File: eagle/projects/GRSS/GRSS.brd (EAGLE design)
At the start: 85 x 47 mm, 33 parts, among them J1 MOL-SL-2-RA, J10 MOL-SL-2-RA, J11 M02PTH, J2 MOL-SL-2-RA, J3 MOL-SL-2-RA, J4 MOL-SL-2-RA, J5 MOL-SL-2-RA, J6 MOL-SL-2-RA, J7 MOL-SL-2-RA, J8 MOL-SL-2-RA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

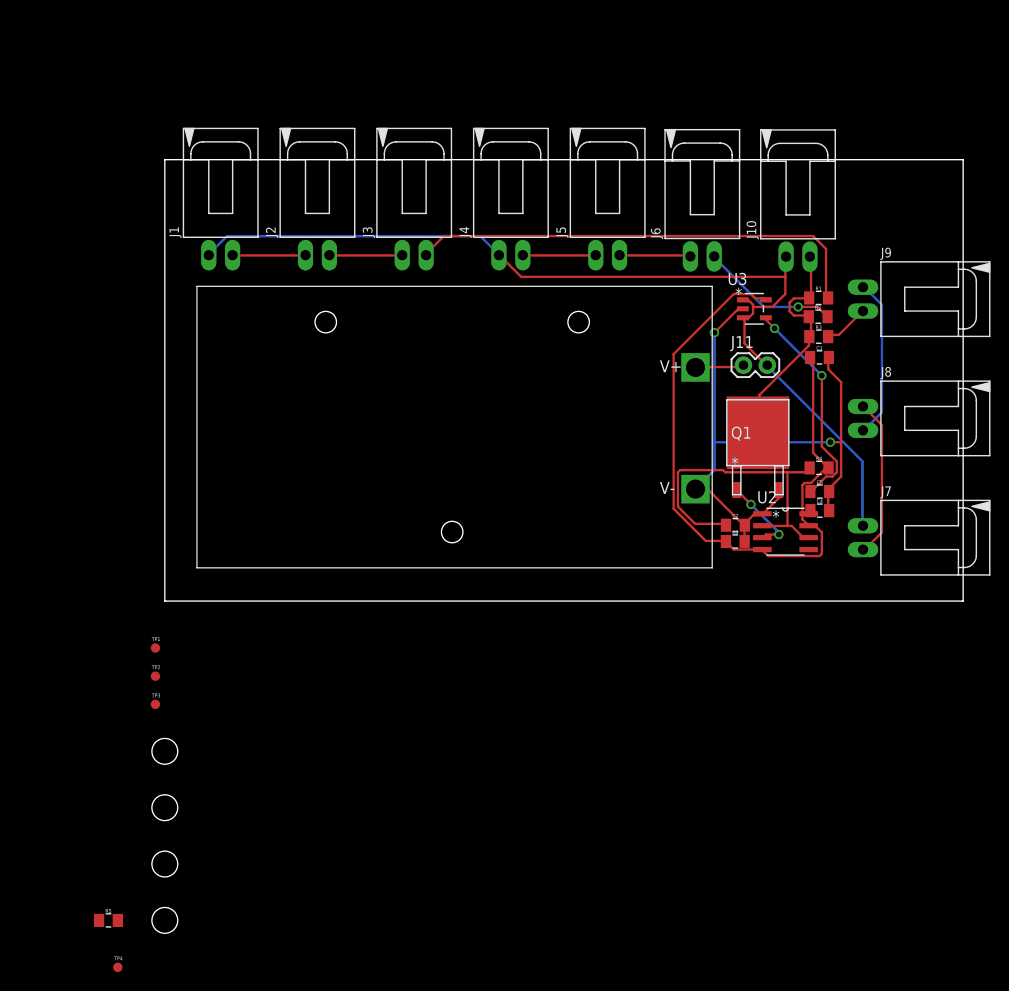
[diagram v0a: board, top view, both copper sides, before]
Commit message: Added 3.3,4.7uF,1k to lib, Schematic now at RevB, Battery flipped to bottom of board
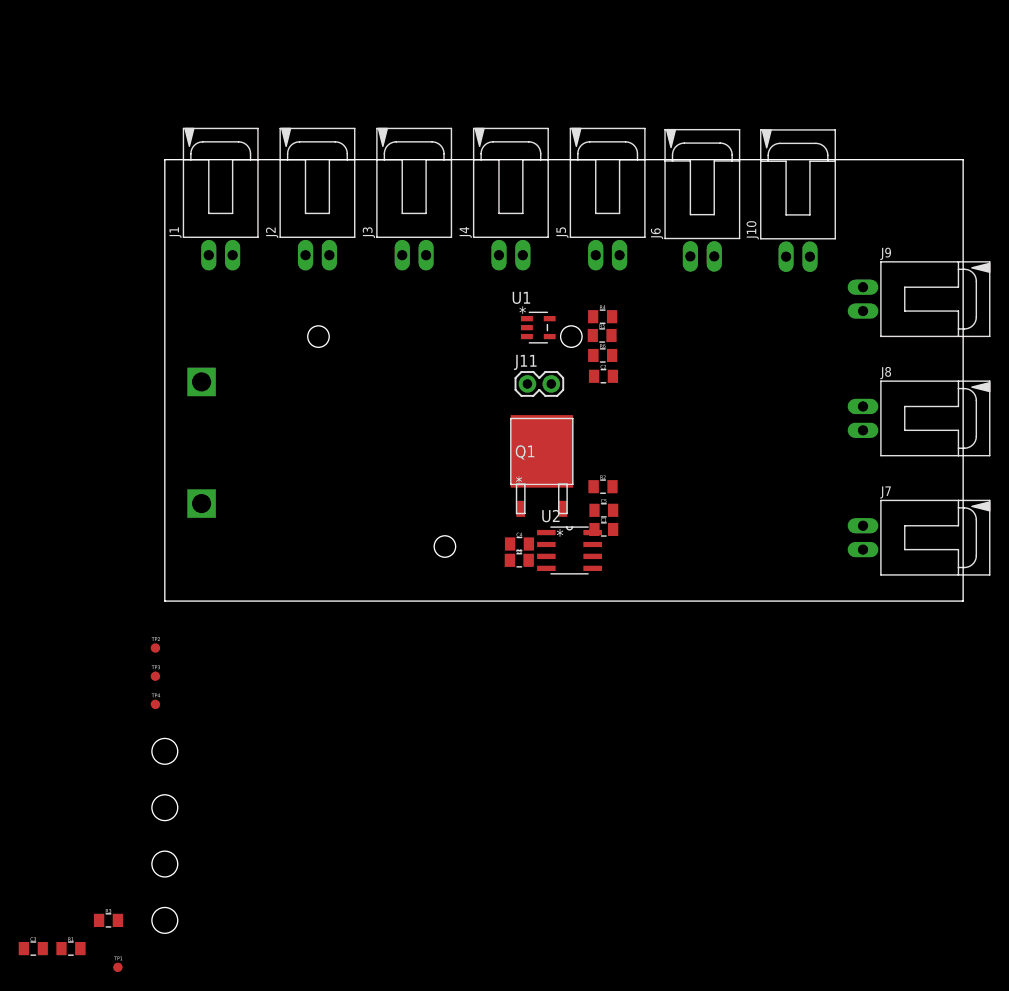
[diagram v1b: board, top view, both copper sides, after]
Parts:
- removed U3: LP2985AIM5-4.5/NOPB, grss:MF05A
- added C6: 3.3uF, grss:C0805
- added R6: 100, grss:R0805
- added U1: LP2985AIM5-4.5/NOPB, grss:MF05A
- C1: value 0.1uF -> 1uF
- C2: value 10uF -> 0.1uF
- C3: value 2.2uF -> 1uF
- C4: value 1uF -> 10uF
- R1: value 100 -> 1k
- R2: value 100 -> 470k
- R3: value 100 -> 4.7k
- R4: value 240k -> 100
- R5: value 4.7k -> 100
- TP1: value (none) -> GND
- TP2: value (none) -> 4V5
- TP3: value (none) -> 555OUT
- TP4: value (none) -> VD
- moved R1 105.5 mm to (-10.0, -37.0)
- moved R3 97.9 mm to (-6.00, -34.0)
- moved C3 86.4 mm to (-14.0, -37.0)
- moved R5 81.5 mm to (46.6, 28.3)
- moved BATT 53.6 mm to (57.0, 2.00), flipped to the bottom
- moved TP1 34.2 mm to (-5.00, -39.0)
- moved C4 32.2 mm to (37.8, 6.07)
- moved C1 29.4 mm to (46.7, 7.63)
- moved R2 29.2 mm to (46.7, 12.2)
- moved TP4 28.3 mm to (-1.00, -11.0)
- moved R4 28.1 mm to (46.6, 30.3)
- moved J11 23.1 mm to (38.6, 23.1)
- moved Q1 23.1 mm to (40.1, 15.9)
- moved U2 23.1 mm to (43.1, 5.39)
- moved C5 23.1 mm to (46.7, 9.66)
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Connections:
- new net DIS: R1.1, R2.2, U2.7
- net 4V5: now also C2.1, C6.1, R1.2, TP2.TP, U1.5; no longer C1.1, R4.2, TP1.TP, U2.7, U3.5
- net 555OUT: now also R3.2, TP3.TP; no longer R5.2, TP2.TP
- net 9V0: now also C1.1, U1.1, U1.3; no longer C4.1, U3.1, U3.3
- net BP: now also U1.4; no longer U3.4
- net GND: now also C6.2, R3.1, TP1.TP, U1.2; no longer R5.1, TP4.TP, U3.2
- net RES123: now also R4.2; no longer R1.2
- net RES456: now also R5.2; no longer R2.2
- net RES789: now also R6.2; no longer R3.2
- net THRTRIG: now also C4.1, R2.1; no longer C2.1, R4.1
- net VD: now also R4.1, R5.1, R6.1, TP4.TP; no longer R1.1, R2.1, R3.1, TP3.TP
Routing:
- net 9V0: track 103.0 -> 0.00 mm
- net 4V5: track 71.9 -> 0.00 mm
- net GND: track 67.0 -> 0.00 mm, vias 2 -> 0
- net RES123: track 49.4 -> 0.00 mm
- net THRTRIG: track 35.7 -> 0.00 mm
- net VD: track 25.0 -> 0.00 mm
- net BP: track 23.2 -> 0.00 mm, vias 2 -> 0
- net LED78: track 17.0 -> 0.00 mm
- net LED89: track 17.0 -> 0.00 mm
- net RES456: track 14.8 -> 0.00 mm, vias 1 -> 0
- net 555OUT: track 8.47 -> 0.00 mm, vias 2 -> 0
- net LED45: track 7.77 -> 0.00 mm
- net LED23: track 7.77 -> 0.00 mm
- net LED12: track 7.77 -> 0.00 mm
- net LED56: track 7.57 -> 0.00 mm
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
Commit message: rough initial placement... 66x50mm
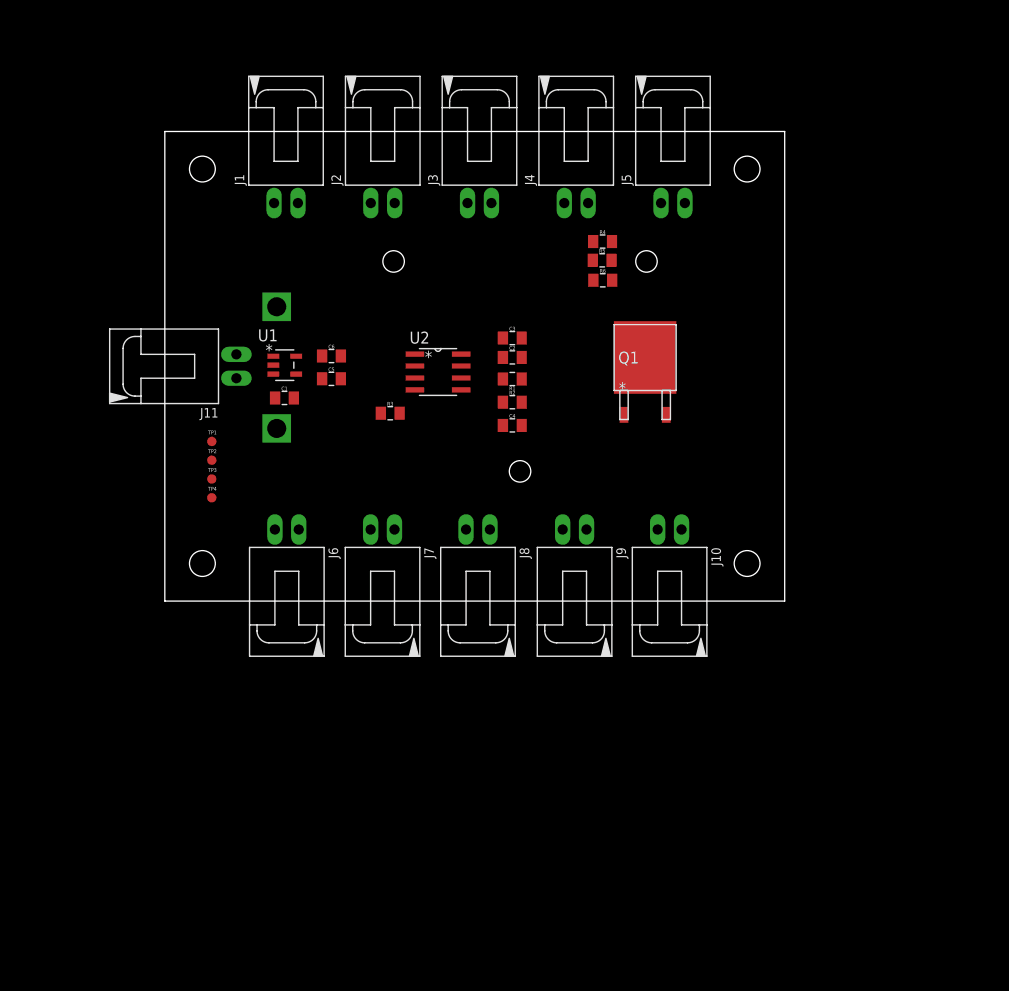
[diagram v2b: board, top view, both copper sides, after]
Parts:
- J11: value M02PTH -> MOL-SL-2-RA; device grss:1X02 -> grss:MOLSL-2-RA
- moved H4 101.2 mm to (62.0, 46.0)
- moved C3 82.6 mm to (37.0, 28.0)
- moved R1 76.7 mm to (37.0, 23.6), turned to 180 degrees
- moved H3 74.1 mm to (4.00, 46.0)
- moved H2 67.2 mm to (62.0, 4.00)
- moved J6 62.6 mm to (13.0, 0.00), turned to 180 degrees
- moved R3 61.8 mm to (24.0, 20.0)
- moved J7 59.2 mm to (23.2, 0.00), turned to 180 degrees
- moved TP1 56.9 mm to (5.00, 17.0)
- moved J8 52.4 mm to (33.3, 0.00), turned to 180 degrees
- moved J9 50.0 mm to (43.6, 0.00), turned to 180 degrees
- moved J10 46.4 mm to (53.7, 0.00), turned to 180 degrees
- moved J11 38.7 mm to (0.00, 25.0), turned to 90 degrees
- moved C1 36.8 mm to (12.7, 21.6)
- moved C5 32.2 mm to (17.7, 23.7)
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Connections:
- removed net 9V0SRC: BATT.V+, J11.1
- new net 9VSRC: BATT.V+, J11.2
- net 9V0: now also J11.1; no longer J11.2
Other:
- board size 85 x 47 mm -> 66 x 50 mm

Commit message: Updated LED series resistor to 200 ohms
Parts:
- R4, R5, R6: value 100 -> 200
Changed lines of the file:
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@@
 <attribute name="MANUFACTURER_PN" value="STD12NF06LT4" x="51.14" y="25.93" size="1.778" layer="27" display="off"/>
 </element>
-<element name="R4" library="grss" package="R0805" value="100" x="46.615" y="38.28">
+<element name="R4" library="grss" package="R0805" value="200" x="46.615" y="38.28">
 <attribute name="POWER" value="1/2W" x="46.615" y="38.28" size="1.778" layer="27" display="off"/>
-<attribute name="VENDOR_PN" value="P16057CT-ND" x="46.615" y="38.28" size="1.778" layer="27" display="off"/>
+<attribute name="VENDOR_PN" value="P16064CT-ND" x="46.615" y="38.28" size="1.778" layer="27" display="off"/>
 <attribute name="VENDOR" value="Digi-key" x="46.615" y="38.28" size="1.778" layer="27" display="off"/>
 <attribute name="MANUFACTURER" value="Panasonic" x="46.615" y="38.28" size="1.778" layer="27" display="off"/>
-<attribute name="MANUFACTURER_PN" value="ERJ-P06F1000V" x="46.615" y="38.28" size="1.778" layer="27" display="off"/>
+<attribute name="MANUFACTURER_PN" value="ERJ-P06F2000V" x="46.615" y="38.28" size="1.778" layer="27" display="off"/>
 <attribute name="TOLERANCE" value="1%" x="46.615" y="38.28" size="1.778" layer="27" display="off"/>
 </element>
-<element name="R5" library="grss" package="R0805" value="100" x="46.567" y="36.28">
+<element name="R5" library="grss" package="R0805" value="200" x="46.567" y="36.28">
 <attribute name="POWER" value="1/2W" x="46.567" y="36.28" size="1.778" layer="27" display="off"/>
-<attribute name="VENDOR_PN" value="P16057CT-ND" x="46.567" y="36.28" size="1.778" layer="27" display="off"/>
+<attribute name="VENDOR_PN" value="P16064CT-ND" x="46.567" y="36.28" size="1.778" layer="27" display="off"/>
 <attribute name="VENDOR" value="Digi-key" x="46.567" y="36.28" size="1.778" layer="27" display="off"/>
 <attribute name="MANUFACTURER" value="Panasonic" x="46.567" y="36.28" size="1.778" layer="27" display="off"/>
-<attribute name="MANUFACTURER_PN" value="ERJ-P06F1000V" x="46.567" y="36.28" size="1.778" layer="27" display="off"/>
+<attribute name="MANUFACTURER_PN" value="ERJ-P06F2000V" x="46.567" y="36.28" size="1.778" layer="27" display="off"/>
 <attribute name="TOLERANCE" value="1%" x="46.567" y="36.28" size="1.778" layer="27" display="off"/>
 </element>
-<element name="R6" library="grss" package="R0805" value="100" x="46.63" y="34.153">
+<element name="R6" library="grss" package="R0805" value="200" x="46.63" y="34.153">
 <attribute name="POWER" value="1/2W" x="46.63" y="34.153" size="1.778" layer="27" display="off"/>
-<attribute name="VENDOR_PN" value="P16057CT-ND" x="46.63" y="34.153" size="1.778" layer="27" display="off"/>
+<attribute name="VENDOR_PN" value="P16064CT-ND" x="46.63" y="34.153" size="1.778" layer="27" display="off"/>
 <attribute name="VENDOR" value="Digi-key" x="46.63" y="34.153" size="1.778" layer="27" display="off"/>
 <attribute name="MANUFACTURER" value="Panasonic" x="46.63" y="34.153" size="1.778" layer="27" display="off"/>
-<attribute name="MANUFACTURER_PN" value="ERJ-P06F1000V" x="46.63" y="34.153" size="1.778" layer="27" display="off"/>
+<attribute name="MANUFACTURER_PN" value="ERJ-P06F2000V" x="46.63" y="34.153" size="1.778" layer="27" display="off"/>
 <attribute name="TOLERANCE" value="1%" x="46.63" y="34.153" size="1.778" layer="27" display="off"/>
 </element>

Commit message: Added Zero ohm resistor on FET drain for sys current meas
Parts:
- added R7: 0.0, grss:R0805
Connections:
- new net ZEROOHM: Q1.2, R7.2
- net GND: now also R7.1; no longer Q1.2
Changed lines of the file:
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@@
 <attribute name="VENDOR" value="Digi-key" x="37" y="28" size="1.778" layer="27" display="off"/>
+</element>
+<element name="R7" library="grss" package="R0805" value="0.0" x="-8" y="-3">
+<attribute name="POWER" value="1/8W" x="-8" y="-3" size="1.778" layer="27" display="off"/>
+<attribute name="TOLERANCE" value="Jumper" x="-8" y="-3" size="1.778" layer="27" display="off"/>
+<attribute name="VENDOR" value="Digi-key" x="-8" y="-3" size="1.778" layer="27" display="off"/>
+<attribute name="MANUFACTURER" value="Panasonic" x="-8" y="-3" size="1.778" layer="27" display="off"/>
+<attribute name="MANUFACTURER_PN" value="ERJ-6GEY0R00V" x="-8" y="-3" size="1.778" layer="27" display="off"/>
+<attribute name="VENDOR_PN" value="P0.0ACT-ND" x="-8" y="-3" size="1.778" layer="27" display="off"/>
 </element>
 </elements>
@@
 <contactref element="C5" pad="2"/>
 <contactref element="C6" pad="2"/>
-<contactref element="Q1" pad="2"/>
 <contactref element="R3" pad="1"/>
 <contactref element="TP1" pad="TP"/>
@@
 <contactref element="C3" pad="2"/>
 <contactref element="C4" pad="2"/>
-<wire x1="11.5508" y1="25.12" x2="38" y2="25.944" width="0" layer="19" extent="1-1"/>
-<wire x1="18.74" y1="23.66" x2="38" y2="25.944" width="0" layer="19" extent="1-1"/>
+<contactref element="R7" pad="1"/>
+<wire x1="38" y1="25.944" x2="38" y2="28" width="0" layer="19" extent="1-1"/>
+<wire x1="38" y1="18.707" x2="38" y2="25.944" width="0" layer="19" extent="1-1"/>
+<wire x1="26.6262" y1="26.295" x2="38" y2="25.944" width="0" layer="19" extent="1-1"/>
+<wire x1="23" y1="20" x2="26.6262" y2="26.295" width="0" layer="19" extent="1-1"/>
+<wire x1="18.74" y1="23.66" x2="23" y2="20" width="0" layer="19" extent="1-1"/>
+<wire x1="18.745" y1="26.089" x2="18.74" y2="23.66" width="0" layer="19" extent="1-1"/>
 <wire x1="13.74" y1="21.628" x2="18.74" y2="23.66" width="0" layer="19" extent="1-1"/>
-<wire x1="53.39" y1="19.8213" x2="18.74" y2="23.66" width="0" layer="19" extent="1-1"/>
-<wire x1="26.6262" y1="26.295" x2="53.39" y2="19.8213" width="0" layer="19" extent="1-1"/>
-<wire x1="38" y1="18.707" x2="26.6262" y2="26.295" width="0" layer="19" extent="1-1"/>
-<wire x1="18.745" y1="26.089" x2="38" y2="18.707" width="0" layer="19" extent="1-1"/>
-<wire x1="11.914" y1="18.382" x2="38" y2="18.707" width="0" layer="19" extent="1-1"/>
-<wire x1="23" y1="20" x2="11.914" y2="18.382" width="0" layer="19" extent="1-1"/>
-<wire x1="5" y1="17" x2="23" y2="20" width="0" layer="19" extent="1-1"/>
-<wire x1="38" y1="28" x2="23" y2="20" width="0" layer="19" extent="1-1"/>
+<wire x1="11.914" y1="18.382" x2="13.74" y2="21.628" width="0" layer="19" extent="1-1"/>
+<wire x1="11.5508" y1="25.12" x2="13.74" y2="21.628" width="0" layer="19" extent="1-1"/>
+<wire x1="5" y1="17" x2="11.914" y2="18.382" width="0" layer="19" extent="1-1"/>
+<wire x1="-9" y1="-3" x2="5" y2="17" width="0" layer="19" extent="1-1"/>
 </signal>
 <signal name="THRTRIG">
@@
 <wire x1="11.914" y1="31.336" x2="7.62" y2="26.27" width="0" layer="19" extent="1-1"/>
 </signal>
+<signal name="ZEROOHM">
+<contactref element="R7" pad="2"/>
+<contactref element="Q1" pad="2"/>
+<wire x1="-7" y1="-3" x2="53.39" y2="19.8213" width="0" layer="19" extent="1-1"/>
+</signal>
 </signals>

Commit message: small placement change
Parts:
- moved R7 58.5 mm to (48.0, 14.0), turned to 90 degrees
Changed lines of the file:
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@@
 <attribute name="VENDOR" value="Digi-key" x="37" y="28" size="1.778" layer="27" display="off"/>
 </element>
-<element name="R7" library="grss" package="R0805" value="0.0" x="-8" y="-3">
-<attribute name="POWER" value="1/8W" x="-8" y="-3" size="1.778" layer="27" display="off"/>
-<attribute name="TOLERANCE" value="Jumper" x="-8" y="-3" size="1.778" layer="27" display="off"/>
-<attribute name="VENDOR" value="Digi-key" x="-8" y="-3" size="1.778" layer="27" display="off"/>
-<attribute name="MANUFACTURER" value="Panasonic" x="-8" y="-3" size="1.778" layer="27" display="off"/>
-<attribute name="MANUFACTURER_PN" value="ERJ-6GEY0R00V" x="-8" y="-3" size="1.778" layer="27" display="off"/>
-<attribute name="VENDOR_PN" value="P0.0ACT-ND" x="-8" y="-3" size="1.778" layer="27" display="off"/>
+<element name="R7" library="grss" package="R0805" value="0.0" x="48" y="14" rot="R90">
+<attribute name="POWER" value="1/8W" x="48" y="14" size="1.778" layer="27" rot="R90" display="off"/>
+<attribute name="TOLERANCE" value="Jumper" x="48" y="14" size="1.778" layer="27" rot="R90" display="off"/>
+<attribute name="VENDOR" value="Digi-key" x="48" y="14" size="1.778" layer="27" rot="R90" display="off"/>
+<attribute name="MANUFACTURER" value="Panasonic" x="48" y="14" size="1.778" layer="27" rot="R90" display="off"/>
+<attribute name="MANUFACTURER_PN" value="ERJ-6GEY0R00V" x="48" y="14" size="1.778" layer="27" rot="R90" display="off"/>
+<attribute name="VENDOR_PN" value="P0.0ACT-ND" x="48" y="14" size="1.778" layer="27" rot="R90" display="off"/>
 </element>
 </elements>
@@
 <wire x1="11.5508" y1="25.12" x2="13.74" y2="21.628" width="0" layer="19" extent="1-1"/>
 <wire x1="5" y1="17" x2="11.914" y2="18.382" width="0" layer="19" extent="1-1"/>
-<wire x1="-9" y1="-3" x2="5" y2="17" width="0" layer="19" extent="1-1"/>
+<wire x1="48" y1="13" x2="5" y2="17" width="0" layer="19" extent="1-1"/>
 </signal>
 <signal name="THRTRIG">
@@
 <contactref element="R7" pad="2"/>
 <contactref element="Q1" pad="2"/>
-<wire x1="-7" y1="-3" x2="53.39" y2="19.8213" width="0" layer="19" extent="1-1"/>
+<wire x1="48" y1="15" x2="53.39" y2="19.8213" width="0" layer="19" extent="1-1"/>
 </signal>
 </signals>

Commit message: Attempt at LDO / 555 Timer solo Layout
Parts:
- moved R3 10.8 mm to (28.0, 30.0), turned to 270 degrees
- moved C3 10.4 mm to (34.0, 38.0), turned to 180 degrees
- moved R2 9.65 mm to (43.8, 28.0), turned to 90 degrees
- moved C2 9.59 mm to (34.0, 35.1), turned to 180 degrees
- moved C4 8.68 mm to (41.7, 26.0), turned to 270 degrees
- moved R1 7.87 mm to (41.6, 30.0), turned to 90 degrees
- moved U2 7.07 mm to (34.1, 29.4)
- moved C5 6.36 mm to (24.0, 24.7), turned to 90 degrees
- moved U1 5.10 mm to (17.8, 26.1)
- moved C1 4.48 mm to (13.4, 26.1)
- moved C6 4.12 mm to (21.8, 26.7), turned to 270 degrees
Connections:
- net N$1 renamed NC
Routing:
- net 4V5: track 0.00 -> 24.2 mm, vias 0 -> 2
- net GND: track 0.00 -> 21.4 mm
- net THRTRIG: track 0.00 -> 13.5 mm
- net 9V0: track 0.00 -> 11.7 mm
- net LED45: track 0.00 -> 7.76 mm
- net LED23: track 0.00 -> 7.76 mm
- net LED12: track 0.00 -> 7.76 mm
- net DIS: track 0.00 -> 7.69 mm
- net BP: track 0.00 -> 5.70 mm
- net 555OUT: track 0.00 -> 3.73 mm

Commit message: LG Route Take 1
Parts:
- moved TP4 45.6 mm to (50.6, 11.7)
- moved TP2 26.0 mm to (28.3, 26.5)
- moved R5 24.8 mm to (41.1, 12.1), turned to 270 degrees
- moved TP3 24.7 mm to (29.4, 16.7)
- moved R6 22.2 mm to (44.1, 12.1), turned to 270 degrees
- moved R4 12.7 mm to (45.9, 25.6), turned to 90 degrees
- moved Q1 9.95 mm to (59.6, 20.7), turned to 270 degrees
- moved R2 6.73 mm to (45.9, 21.6)
- moved R3 6.65 mm to (29.4, 23.5)
- moved U2 6.62 mm to (35.4, 22.9)
- moved C2 6.61 mm to (35.4, 28.6)
- moved C3 6.55 mm to (35.4, 31.6)
- moved R1 6.52 mm to (42.9, 23.6)
- moved C4 6.51 mm to (42.9, 19.6)
- moved R7 4.72 mm to (49.6, 18.4), turned to 0 degrees
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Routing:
- net 9V0: track 11.7 -> 111.2 mm
- net LED56: track 0.00 -> 58.4 mm, vias 0 -> 2
- net VD: track 0.00 -> 45.2 mm
- net 4V5: track 24.2 -> 62.0 mm
- net GND: track 21.4 -> 58.5 mm
- net 555OUT: track 3.73 -> 37.0 mm, vias 0 -> 2
- net RES456: track 0.00 -> 32.6 mm
- net RES123: track 0.00 -> 20.4 mm
- net LED89: track 0.00 -> 18.1 mm
- net LED78: track 0.00 -> 17.3 mm
- net 9VSRC: track 0.00 -> 8.27 mm
- net RES789: track 0.00 -> 4.13 mm
- net ZEROOHM: track 0.00 -> 2.93 mm
- net THRTRIG: track 13.5 -> 14.5 mm
- net DIS: track 7.69 -> 8.42 mm
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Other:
- outline, holes or cut-outs redrawn
